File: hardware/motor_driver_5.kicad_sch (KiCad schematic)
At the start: 15 parts, among them J4 B2B-XH-A(LF)(SN), U3 DRV8701ERGET, U4 DMHT6016LFJ-13

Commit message: Complete Schematic for Power Section
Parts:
- renumbered C28 to C24, C27 to C25, C25 to C26, C26 to C27, R16 to R10, R10 to R12, R14 to R13, R12 to R14, R13 to R15, R17 to R16, R15 to R9
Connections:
- net VM renamed +12V
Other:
- moved on the sheet: C25, C26, C27

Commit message: Organize schematic
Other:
- note added: "Connector"
- note added: "Driver"
- note added: "MOSFET"
- moved on the sheet: C24, C25, C26, C27, J4, R10, R11, R12, R13, R14, R15, R16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

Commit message: Link footprints to Symbols
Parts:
- C24, C25, C26, C27: footprint Package_QFP:LQFP-48_7x7mm_P0.5mm -> STM32F407 Dev Kit Library:C_0805_2012Metric_Pad1.18x1.45mm_HandSolder
- J4: footprint Package_QFP:LQFP-48_7x7mm_P0.5mm -> STM32F407 Dev Kit Library:JST_XH_B2B-XH-A_1x02_P2.50mm_Vertical
- R10, R11, R12, R13, R14, R15, R9: footprint (none) -> STM32F407 Dev Kit Library:R_0805_2012Metric_Pad1.20x1.40mm_HandSolder
- R16: footprint DMHT6016LFJ-13:TRANS_DMHT6016LFJ-13 -> STM32F407 Dev Kit Library:R_0805_2012Metric_Pad1.20x1.40mm_HandSolder
- U3: footprint DRV8701ERGET:QFN50P400X400X100-25N -> STM32F407 Dev Kit Library:QFN-24-1EP_4x4mm_P0.5mm_EP2.7x2.7mm
- U4: footprint DMHT6016LFJ-13:TRANS_DMHT6016LFJ-13 -> STM32F407 Dev Kit Library:V-DFN5045-12
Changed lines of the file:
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@@
 			)
 		)
-		(property "Footprint" "DMHT6016LFJ-13:TRANS_DMHT6016LFJ-13"
+		(property "Footprint" "STM32F407 Dev Kit Library:R_0805_2012Metric_Pad1.20x1.40mm_HandSolder"
 			(at 196.342 101.6 90)
 			(hide yes)
@@
 			)
 		)
-		(property "Footprint" ""
+		(property "Footprint" "STM32F407 Dev Kit Library:R_0805_2012Metric_Pad1.20x1.40mm_HandSolder"
 			(at 67.818 81.28 90)
 			(hide yes)
@@
 			)
 		)
-		(property "Footprint" "Package_QFP:LQFP-48_7x7mm_P0.5mm"
+		(property "Footprint" "STM32F407 Dev Kit Library:C_0805_2012Metric_Pad1.18x1.45mm_HandSolder"
 			(at 169.8752 88.9 0)
 			(hide yes)
@@
 			)
 		)
-		(property "Footprint" "Package_QFP:LQFP-48_7x7mm_P0.5mm"
+		(property "Footprint" "STM32F407 Dev Kit Library:C_0805_2012Metric_Pad1.18x1.45mm_HandSolder"
 			(at 86.0552 119.38 0)
 			(hide yes)
@@
 			)
 		)
-		(property "Footprint" ""
+		(property "Footprint" "STM32F407 Dev Kit Library:R_0805_2012Metric_Pad1.20x1.40mm_HandSolder"
 			(at 74.422 111.76 90)
 			(hide yes)
@@
 			)
 		)
-		(property "Footprint" "DMHT6016LFJ-13:TRANS_DMHT6016LFJ-13"
+		(property "Footprint" "STM32F407 Dev Kit Library:V-DFN5045-12"
 			(at 215.9 82.55 0)
 			(hide yes)
@@
 			)
 		)
-		(property "Footprint" "Package_QFP:LQFP-48_7x7mm_P0.5mm"
+		(property "Footprint" "STM32F407 Dev Kit Library:C_0805_2012Metric_Pad1.18x1.45mm_HandSolder"
 			(at 150.8252 88.9 0)
 			(hide yes)
@@
 			)
 		)
-		(property "Footprint" ""
+		(property "Footprint" "STM32F407 Dev Kit Library:R_0805_2012Metric_Pad1.20x1.40mm_HandSolder"
 			(at 158.242 115.57 90)
 			(hide yes)
@@
 			)
 		)
-		(property "Footprint" ""
+		(property "Footprint" "STM32F407 Dev Kit Library:R_0805_2012Metric_Pad1.20x1.40mm_HandSolder"
 			(at 74.422 101.6 90)
 			(hide yes)
@@
 			)
 		)
-		(property "Footprint" "Package_QFP:LQFP-48_7x7mm_P0.5mm"
+		(property "Footprint" "STM32F407 Dev Kit Library:C_0805_2012Metric_Pad1.18x1.45mm_HandSolder"
 			(at 159.7152 88.9 0)
 			(hide yes)
@@
 			)
 		)
-		(property "Footprint" ""
+		(property "Footprint" "STM32F407 Dev Kit Library:R_0805_2012Metric_Pad1.20x1.40mm_HandSolder"
 			(at 67.818 91.44 90)
 			(hide yes)
@@
 			)
 		)
-		(property "Footprint" ""
+		(property "Footprint" "STM32F407 Dev Kit Library:R_0805_2012Metric_Pad1.20x1.40mm_HandSolder"
 			(at 82.042 95.25 90)
 			(hide yes)
@@
 			)
 		)
-		(property "Footprint" "Package_QFP:LQFP-48_7x7mm_P0.5mm"
+		(property "Footprint" "STM32F407 Dev Kit Library:JST_XH_B2B-XH-A_1x02_P2.50mm_Vertical"
 			(at 209.55 125.73 0)
 			(hide yes)
@@
 			)
 		)
-		(property "Footprint" "DRV8701ERGET:QFN50P400X400X100-25N"
+		(property "Footprint" "STM32F407 Dev Kit Library:QFN-24-1EP_4x4mm_P0.5mm_EP2.7x2.7mm"
 			(at 116.84 99.06 0)
 			(hide yes)
@@
 			)
 		)
-		(property "Footprint" ""
+		(property "Footprint" "STM32F407 Dev Kit Library:R_0805_2012Metric_Pad1.20x1.40mm_HandSolder"
 			(at 167.132 118.11 90)
 			(hide yes)

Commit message: Convert Schematic to PCB
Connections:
- net SN is gone; now on net GND: R16.2, U3.20 (SN)
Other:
- moved on the sheet: R16

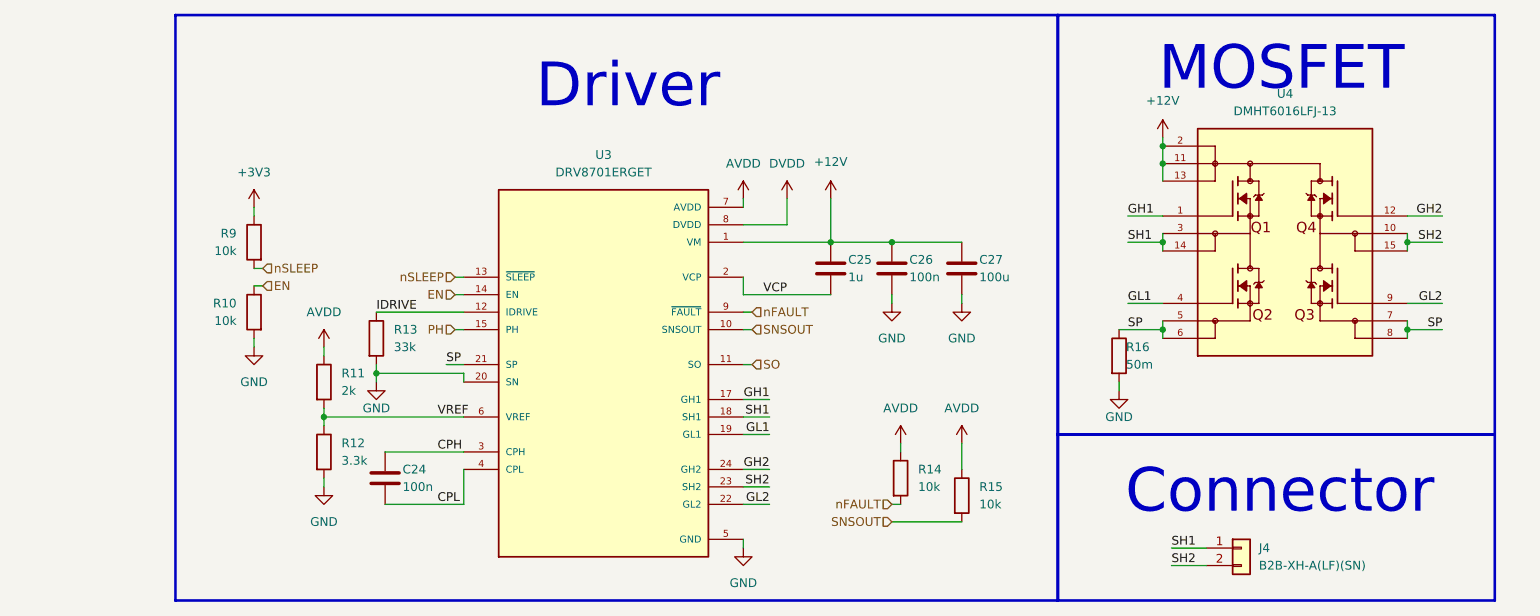
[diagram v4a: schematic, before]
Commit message: Route Ethernet section and add global labels
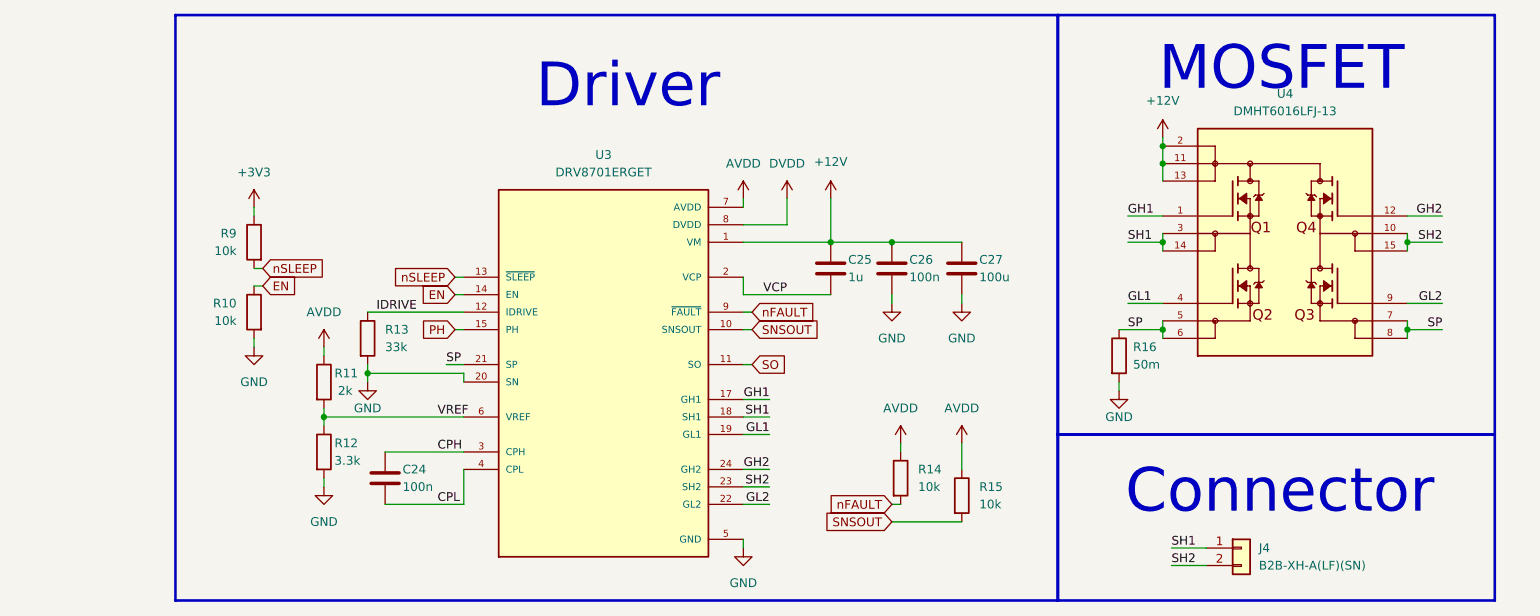
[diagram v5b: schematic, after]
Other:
- moved on the sheet: R13

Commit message: Fix capacitor footprints
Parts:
- C27: footprint STM32F407 Dev Kit Library:C_0805_2012Metric_Pad1.18x1.45mm_HandSolder -> STM32F407 Dev Kit Library:C_1210_3225Metric_Pad1.33x2.70mm_HandSolder
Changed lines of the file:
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@@
 			)
 		)
-		(property "Footprint" "STM32F407 Dev Kit Library:C_0805_2012Metric_Pad1.18x1.45mm_HandSolder"
+		(property "Footprint" "STM32F407 Dev Kit Library:C_1210_3225Metric_Pad1.33x2.70mm_HandSolder"
 			(at 169.8752 88.9 0)
 			(hide yes)
